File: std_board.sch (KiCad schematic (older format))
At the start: 191 parts, among them IC1 ESP32, IC2 ACS712, IC3 L78L05, IC4 AMS1117-V, J1 Jumper, J10 J_DHT11, J11 Jumper, J12 Jumper, J13 J_PRess, J14 Jumper, J15 Jumper, J16 J_PRess, J17 Jumper, J18 Jumper, J19 Jumper, J2 Jumper, J22 Jumper, J24 Jumper, J25 Jumper, J26 Jumper, J27 Jumper, J29 Jumper, J3 Jumper, J31 Jumper, J32 Jumper, J33 Jumper, J34 Jumper, J35 Jumper, J36 Jumper, J37 Jumper, J38 Jumper, J39 Jumper, J4 Jumper, J40 Jumper, J41 Jumper, J42 Jumper, J43 Jumper, J44 Jumper, J45 Jumper, J5 Jumper, J6 J_PRess, J7 Jumper, J8 Jumper, J9 Jumper, T1 TRIAC_Micro, T2 TRIAC_Micro, T3 TRIAC_Micro, T4 NPN, T5 NPN, T6 NPN, T7 NPN, T8 PNP, T9 NPN, U1 LNK306

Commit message: updates on circuit board and readme file
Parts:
- removed IC1: ESP32, thmalmeida:ESP32_DEVKIT, symbol std_board-rescue:ESP32-thmalmeida
- removed Rectifier1: Bridge_Rectifier, Diode_SMD:Diode_Bridge_Diotec_SO-DIL-Slim, symbol std_board-rescue:Bridge_Rectifier-thmalmeida
- added IC1: ESP32, thmalmeida:ESP32_DEVKIT, symbol thmalmeida:ESP32
- added Rectifier1: DF10S, Package_TO_SOT_SMD:TO-269AA, symbol thmalmeida:Bridge_Rectifier
- C12, C13, C14, C15: value 47 nF -> 10 nF
- C22, C23, C26, C29, C7: footprint thmalmeida:C3_elec_5x4.5_pth -> thmalmeida:C4_elec_7x6.7_pth
- J38: Spice_Model (none) -> Jumper; Spice_Netlist_Enabled (none) -> Y; Spice_Primitive (none) -> X
- R17, R18, R31, R32: value 680 k -> 560 k
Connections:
- net labels added: P10, P11, P12, P13, P15, P33, USB_RX, USB_TX, V_input
- net labels removed: 3V3, L01, L02, L03, L04, L05, L06, L07, L08, L09, L10, L11, L12, L13, L14, L15, R01, R02, R03, R04, R05, R06, R07, R08, R09, R10, R11, R12, R13, R14, R15, R16, R17, Vac_input
- wire segments 562 -> 573
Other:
- note added: "-> V_input = 5 VDC\n-> V_input = [9 - 40] VDC\n-> V_input = [12 - 24] VAC\n-> V_input = [85 -265] VAC"
- note added: "AC load driver"
- note added: "Corner holes for screws"
- note added: "Digital temperature sensor\n (DS18B20)"
- note added: "ESP32, MH-ET live mini board"
- note added: "High-Side, Buck-Direct Feedback"
- note added: "Key features described by manufacturer\n\n1. Output referenced to input;\n2. Positive output (Vo in C point) with respect to -V_input;\n3. Step down -Vo < V_input;\n4. Low cost direct feedback (+-10% typ.);\n5. Requires an output load to maintain regulation."
- note added: "Power circuit protection"
- note added: "RTC DS3231"
- note removed: "Buck"
- note removed: "Circuito de Proteção"
- note removed: "DS3231"
- note removed: "Sensor temperatura (DS18B20)"
- moved on the sheet: +5V_In2, 24Vac_In1, C1, C10, C11, C2, C21, C25, C3, C4, C5, C6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

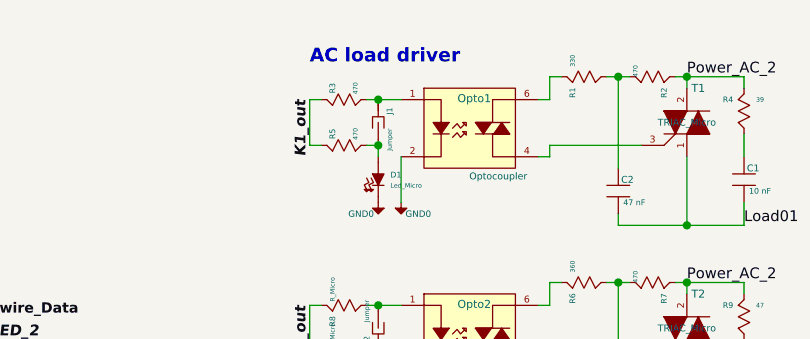
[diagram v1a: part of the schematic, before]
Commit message: AC load explanation
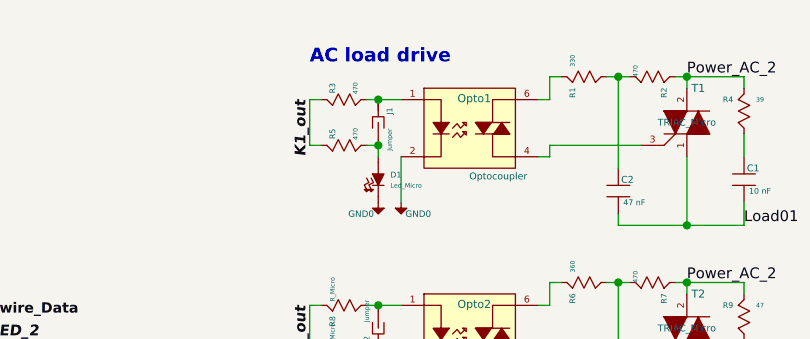
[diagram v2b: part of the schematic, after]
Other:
- note added: "AC load drive"
- note removed: "AC load driver"
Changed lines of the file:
@@
 	800  3550 850  3550
 Text Notes 8950 700  0    60   ~ 12
-AC load driver
+AC load drive
 Wire Wire Line
 	1750 7150 1750 7250

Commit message: TODO list added on REAME.md
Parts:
- AC_Output1, LevelSens_1: symbol thmalmeida:CONN_5X1 -> std_board-rescue:CONN_5X1-thmalmeida
- C10, C11, C8, C9: value 100 nF -> 47 nF
- C22, C23, C24, C26, C27, C29, C7: symbol thmalmeida:CP_Micro -> std_board-rescue:CP_Micro-thmalmeida
- DS3231_1: symbol std_board-rescue:CONN_6X1-thmalmeida -> std_board-rescue:CONN_6X1-thmalmeida-std_board-rescue
- IC1: symbol thmalmeida:ESP32 -> std_board-rescue:ESP32-thmalmeida
- IC3: symbol thmalmeida:L78L05 -> std_board-rescue:L78L05-thmalmeida
- IC4: symbol thmalmeida:AMS1117-V -> std_board-rescue:AMS1117-V-thmalmeida
- Inputs1: symbol thmalmeida:CONN_6X1 -> std_board-rescue:CONN_6X1-thmalmeida
- JTAG1: symbol thmalmeida:JTAG_CONN-06_adapted -> std_board-rescue:JTAG_CONN-06_adapted-thmalmeida
- L1, L2, L4: symbol thmalmeida:L_Micro -> std_board-rescue:L_Micro-thmalmeida
- LS1, LS2: symbol thmalmeida:I_sens -> std_board-rescue:I_sens-thmalmeida
- R20, R21, R22, R23: value 100 k -> 56 k
- R42: value 500 k -> 470 k
- R58: value 3.3 k -> 3.9 k
- Rectifier1: symbol thmalmeida:Bridge_Rectifier -> std_board-rescue:Bridge_Rectifier-thmalmeida
- T8: symbol thmalmeida:PNP -> std_board-rescue:PNP-thmalmeida
- U1: symbol thmalmeida:LNK306 -> std_board-rescue:LNK306-thmalmeida
- Voltimeter_DSO1, currentSource_1: symbol thmalmeida:Connector_2 -> std_board-rescue:Connector_2-thmalmeida
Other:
- note added: "Vrms = 127 V: R42 = 460 k and R58 = 3.9 k"
- note added: "Vrms = 220 V: R42 = 460 k and R58 = 3.9 k"
- moved on the sheet: +5V_In2, D4, J15, J16, J45, R42, R45, R58, R59

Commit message: voltage sensor new structure part 1
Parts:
- removed Voltimeter_DSO1: Voltimeter, TerminalBlock:TerminalBlock_bornier-2_P5.08mm, symbol std_board-rescue:Connector_2-thmalmeida
- added J20, J21, J23: Jumper, thmalmeida:J_0603, symbol std_board-rescue:Jumper-thmalmeida
- added R64: 220 k, Resistor_SMD:R_0805_2012Metric, symbol std_board-rescue:R_Micro-thmalmeida
- AC_Output1: footprint TerminalBlock:TerminalBlock_bornier-5_P5.08mm -> TerminalBlock:TerminalBlock_bornier-6_P5.08mm; symbol std_board-rescue:CONN_5X1-thmalmeida -> std_board-rescue:CONN_6X1-thmalmeida
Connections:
- net Phase_R is gone; now on an unnamed net: J15.2 (B)
- net Common: now also AC_Output1.5, J23.2 (B), R64.1 (A); no longer AC_Output1.1
- net GND: no longer R58.2 (B)
- net Load01: now also AC_Output1.1, J20.1 (A); no longer AC_Output1.5
- net Load02: now also AC_Output1.2; no longer AC_Output1.4
- net Power_AC: now also AC_Output1.4; no longer AC_Output1.2
- net Power_AC_2: now also J15.1 (A)
- net at J45.2 (B), R42.1 (A): now also J20.2 (B), J21.2 (B); no longer J15.1 (A)
- net Neutro: no longer names the net of C24.1, R45.2 (B), R59.1 (A)
- net Neutro: now also R58.2 (B), J23.1 (A), R64.2 (B)
- new net V_external: AC_Output1.6, J21.1 (A)
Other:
- note added: "Common can be\nneutro or one\nreference phase"
- note removed: "Vrms = 220 V: R42 = 460 k and R58 = 3.9 k"
- moved on the sheet: +5V_In2, C24, D4, J15, J16, J45, R42, R45, R58, R59

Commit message: voltage sensor: calculated resistors
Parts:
- removed J27, J29: Jumper, thmalmeida:J_0603, symbol std_board-rescue:Jumper-thmalmeida
- removed T8: PNP, Package_TO_SOT_THT:TO-92, symbol std_board-rescue:PNP-thmalmeida
- added T8: PNP_2N3906, Package_TO_SOT_THT:TO-92, symbol thmalmeida:PNP_TO-92
- Inputs1: value CONN_6X1 -> CONN_5X1; footprint TerminalBlock:TerminalBlock_bornier-6_P5.08mm -> TerminalBlock:TerminalBlock_bornier-5_P5.08mm; symbol std_board-rescue:CONN_6X1-thmalmeida -> std_board-rescue:CONN_5X1-thmalmeida
- R19: value 33 k -> 47 k
- R24: value 1 k -> 2.2 k
- R42: value 470 k -> 680 k
- R58: value 3.9 k -> 3.3 k
- T4, T5, T6, T7, T9: value NPN -> NPN_MMBT222A
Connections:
- net P33 is gone; now on net K3_in: IC1.33 (Wire_SDA/GPIO21_(35))
- net K1_in: now also C8.1 (A), Inputs1.2, R20.2 (B); no longer C9.1 (A), Inputs1.4, R21.2 (B)
- net K2_in: now also C9.1 (A), R21.2 (B); no longer C10.1 (A), R22.2 (B)
- net K3_in: now also C10.1 (A), Inputs1.4, R22.2 (B); no longer C11.1 (A), Inputs1.2, R23.2 (B)
- net L1_in: now also J4.1 (A), J7.2 (B), R17.2 (B), T4.3 (C); no longer J12.1 (A), J22.2 (B), R32.1 (A), T7.3 (C)
- net L1_probe: now also C12.1 (A), J4.2 (B), LevelSens_1.2, R25.1 (A), R27.1 (A); no longer C15.1 (A), J12.2 (B), LevelSens_1.1, R35.1 (A), R37.1 (A)
- net L2_in: now also J26.2 (B), J5.1 (A), R18.2 (B), T5.3 (C); no longer J11.1 (A), J25.2 (B), R31.1 (A), T6.3 (C)
- net L2_probe: now also C13.1 (A), J5.2 (B), LevelSens_1.3, R26.1 (A), R28.1 (A); no longer C14.1 (A), J11.2 (B), LevelSens_1.2, R34.1 (A), R36.1 (A)
- net L3_in: now also J11.1 (A), J25.2 (B), R31.1 (A), T6.3 (C); no longer J26.2 (B), J5.1 (A), R18.2 (B), T5.3 (C)
- net L3_probe: now also C14.1 (A), J11.2 (B), LevelSens_1.4, R34.1 (A), R36.1 (A); no longer C13.1 (A), J5.2 (B), LevelSens_1.3, R26.1 (A), R28.1 (A)
- net L4_in: now also J12.1 (A), J22.2 (B), R32.1 (A), T7.3 (C); no longer J4.1 (A), J7.2 (B), R17.2 (B), T4.3 (C)
- net L4_probe: now also C15.1 (A), J12.2 (B), LevelSens_1.5, R35.1 (A), R37.1 (A); no longer C12.1 (A), J4.2 (B), LevelSens_1.4, R25.1 (A), R27.1 (A)
- net T1_in: now also C11.1 (A), R23.2 (B); no longer C8.1 (A), R20.2 (B)
- net at D7.2 (-Cathode), J9.1 (A): now also LevelSens_1.1; no longer LevelSens_1.5
- net at R24.1 (A): now also T8.2 (B)
- net at J34.2 (B), J37.2 (B), R19.2 (B): now also T8.1 (E)
- net at currentSource_1.1 (S1): now also T8.3 (C)
- removed net T2_in: Inputs1.6
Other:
- note added: "Fórmula: R1/(R2+R1)*Vrms*sqrt(2)+3.3/2"
- note added: "Vmax read = 138 Vrms"
- note added: "Vmax read = 241 Vrms"
- note added: "Vrms = 220 V: R42 = 680 k and R58 = 3.3 k"
- moved on the sheet: C10, C11, C8, C9, R20, R21, R22, R23

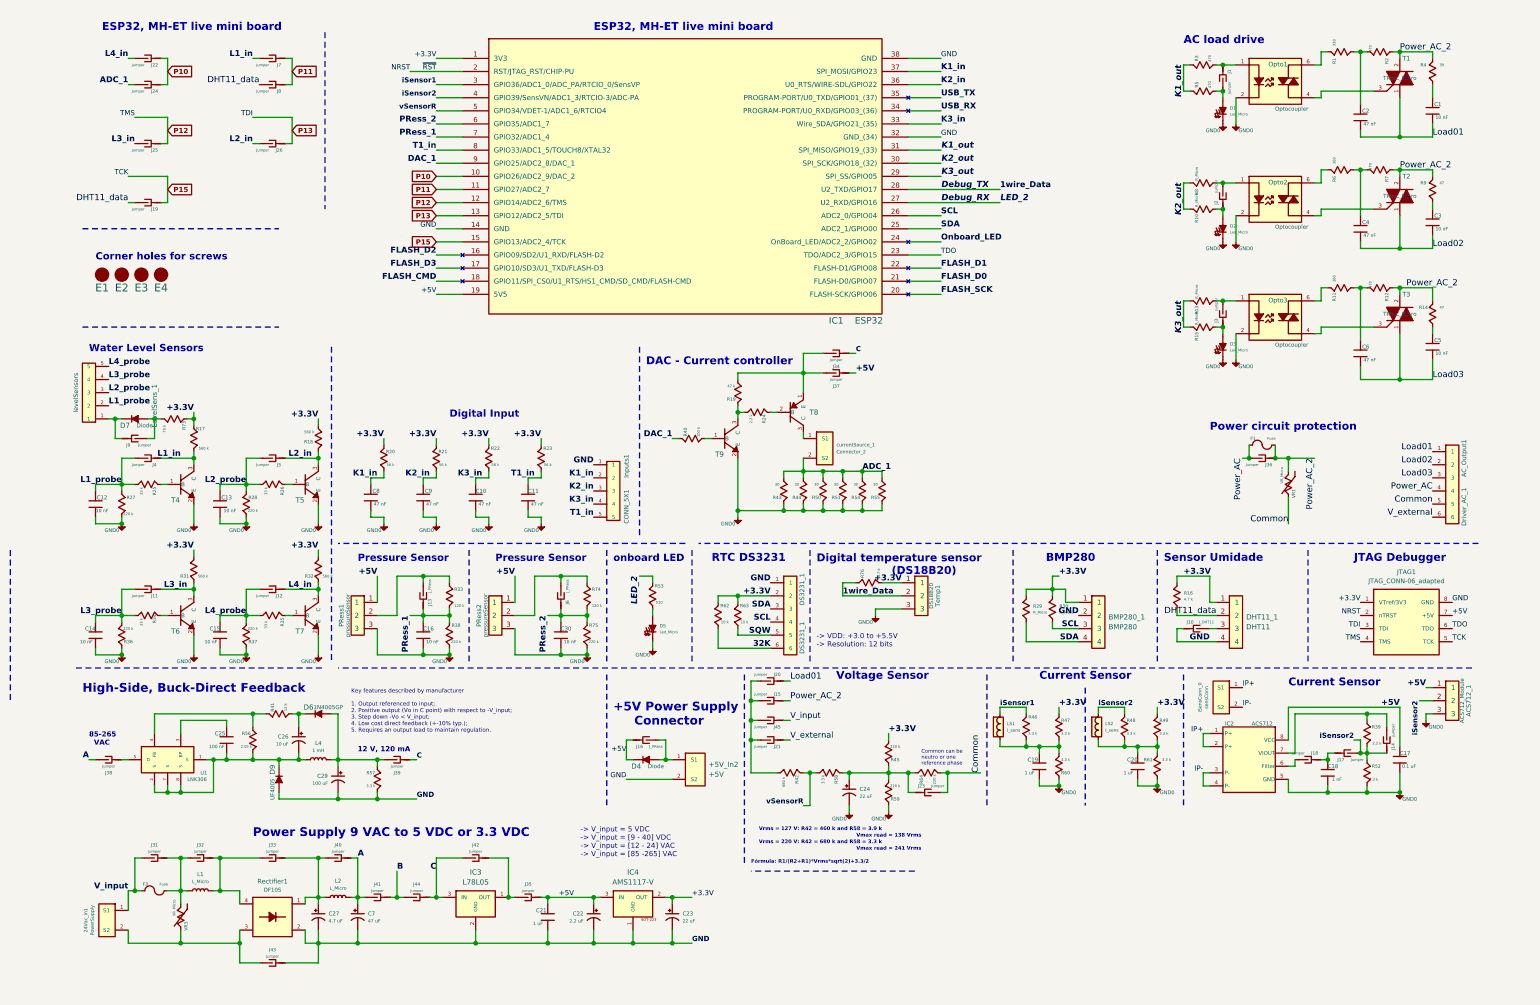
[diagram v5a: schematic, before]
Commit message: fixed voltage divider of pressure circuit design
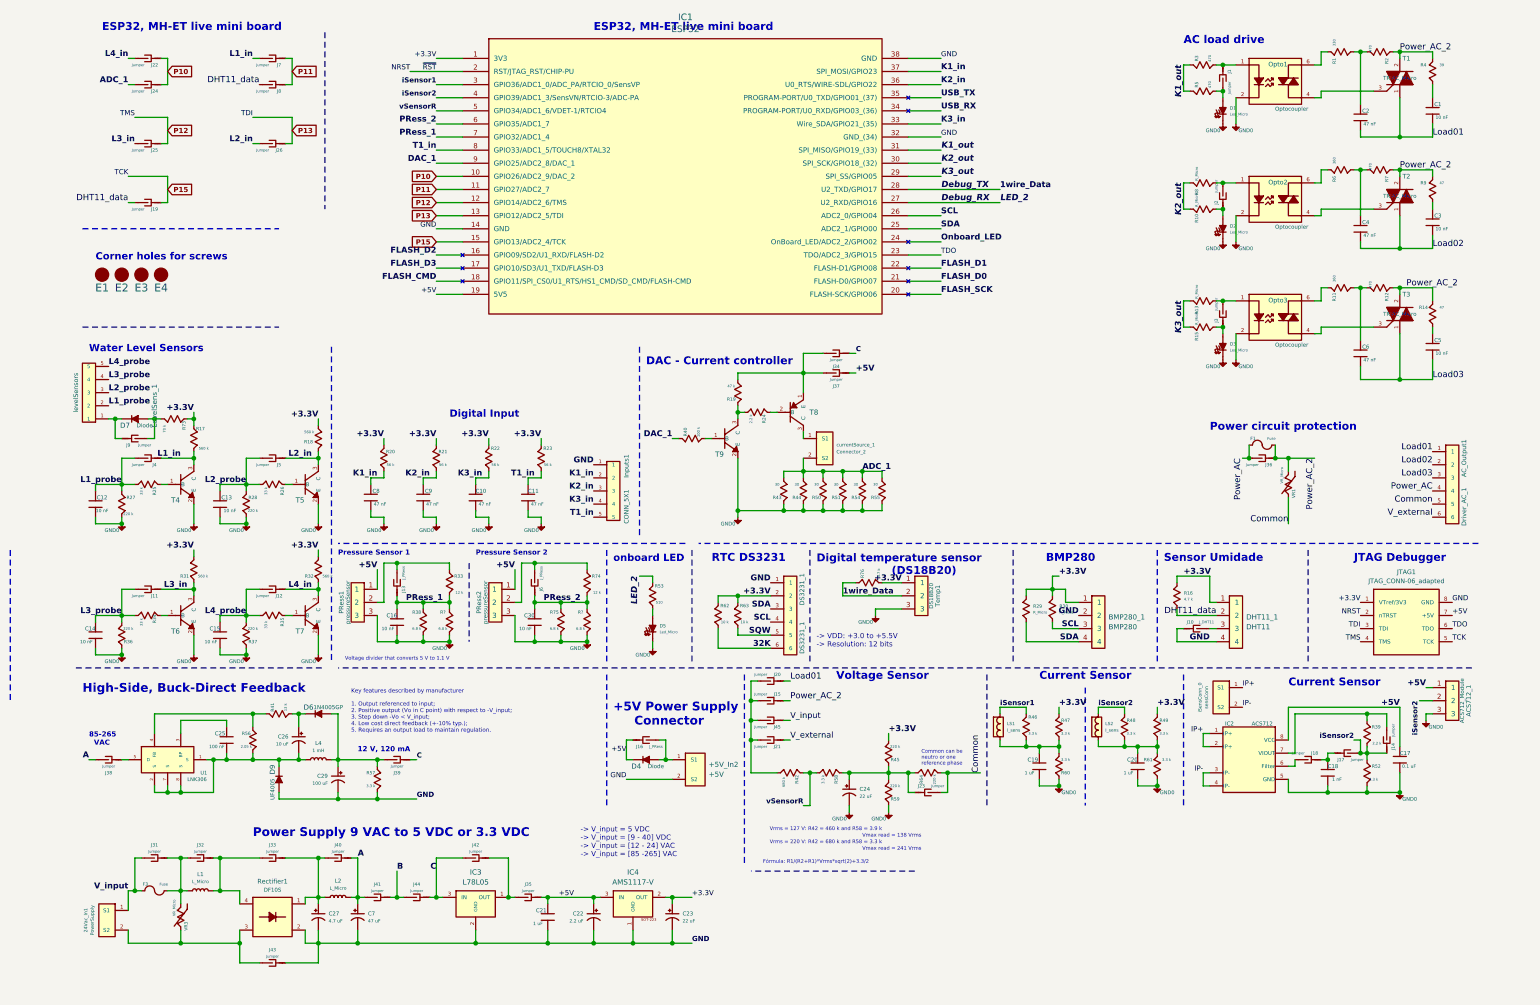
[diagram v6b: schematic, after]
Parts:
- removed IC1: ESP32, thmalmeida:ESP32_DEVKIT, symbol std_board-rescue:ESP32-thmalmeida
- added IC1: ESP32, thmalmeida:ESP32_DEVKIT, symbol thmalmeida:ESP32
- added R? (x2): 6.8 k, Resistor_SMD:R_0805_2012Metric, symbol std_board-rescue:R_Micro-thmalmeida
- R33, R74: value 120 k -> 12 k
- R38, R75: value 220 k -> 6.8 k
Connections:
- net +3.3V: now also IC1.1 (3V3)
- net +5V: now also IC1.19 (5V5)
- net 1wire_Data: now also IC1.28 (U2_TXD/GPIO17)
- net DAC_1: now also IC1.9 (GPIO25/ADC2_8/DAC_1)
- net Debug_RX: now also IC1.27 (U2_RXD/GPIO16)
- net FLASH_CMD: now also IC1.18 (GPIO11/SPI_CS0/U1_RTS/HS1_CMD/SD_CMD/FLASH-CMD)
- net FLASH_D0: now also IC1.21 (FLASH-D0/GPIO07)
- net FLASH_D1: now also IC1.22 (FLASH-D1/GPIO08)
- net FLASH_D2: now also IC1.16 (GPIO09/SD2/U1_RXD/FLASH-D2)
- net FLASH_D3: now also IC1.17 (GPIO10/SD3/U1_TXD/FLASH-D3)
- net FLASH_SCK: now also IC1.20 (FLASH-SCK/GPIO06)
- net GND: now also IC1.14 (GND), IC1.32 (GND_(34)), IC1.38 (GND), R?.2 (B), R?.2 (B)
- net K1_in: now also IC1.37 (SPI_MOSI/GPIO23)
- net K1_out: now also IC1.31 (SPI_MISO/GPIO19_(33))
- net K2_in: now also IC1.36 (U0_RTS/WIRE-SDL/GPIO22)
- net K2_out: now also IC1.30 (SPI_SCK/GPIO18_(32))
- net K3_in: now also IC1.33 (Wire_SDA/GPIO21_(35))
- net K3_out: now also IC1.29 (SPI_SS/GPIO05)
- net NRST: now also IC1.2 (RST/JTAG_RST/CHIP-PU)
- net Onboard_LED: now also IC1.24 (OnBoard_LED/ADC2_2/GPIO02)
- net P10: now also IC1.10 (GPIO26/ADC2_9/DAC_2)
- net P11: now also IC1.11 (GPIO27/ADC2_7)
- net P12: now also IC1.12 (GPIO14/ADC2_6/TMS)
- net P13: now also IC1.13 (GPIO12/ADC2_5/TDI)
- net P15: now also IC1.15 (GPIO13/ADC2_4/TCK)
- net PRess_1: now also IC1.7 (GPIO32/ADC1_4), R?.1 (A)
- net PRess_2: now also IC1.6 (GPIO35/ADC1_7), R?.1 (A)
- net SCL: now also IC1.26 (ADC2_0/GPIO04)
- net SDA: now also IC1.25 (ADC2_1/GPIO00)
- net T1_in: now also IC1.8 (GPIO33/ADC1_5/TOUCH8/XTAL32)
- net TDO: now also IC1.23 (TDO/ADC2_3/GPIO15)
- net USB_RX: now also IC1.34 (PROGRAM-PORT/U0_RXD/GPIO03_(36))
- net USB_TX: now also IC1.35 (PROGRAM-PORT/U0_TXD/GPIO01_(37))
- net iSensor1: now also IC1.3 (GPIO36/ADC1_0/ADC_PA/RTCIO_0/SensVP)
- net iSensor2: now also IC1.4 (GPIO39/ADC1_3/SensVN/RTCIO-3/ADC-PA)
- net vSensorR: now also IC1.5 (GPIO34/ADC1_6/VDET-1/RTCIO4)
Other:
- note added: "Pressure Sensor 1"
- note added: "Pressure Sensor 2"
- note added: "Voltage divider that converts 5 V to 1.1 V"
- note removed: "Pressure Sensor"
- moved on the sheet: C16, C30, J13, J6, PRess1, PRess2, R33, R38, R74, R75

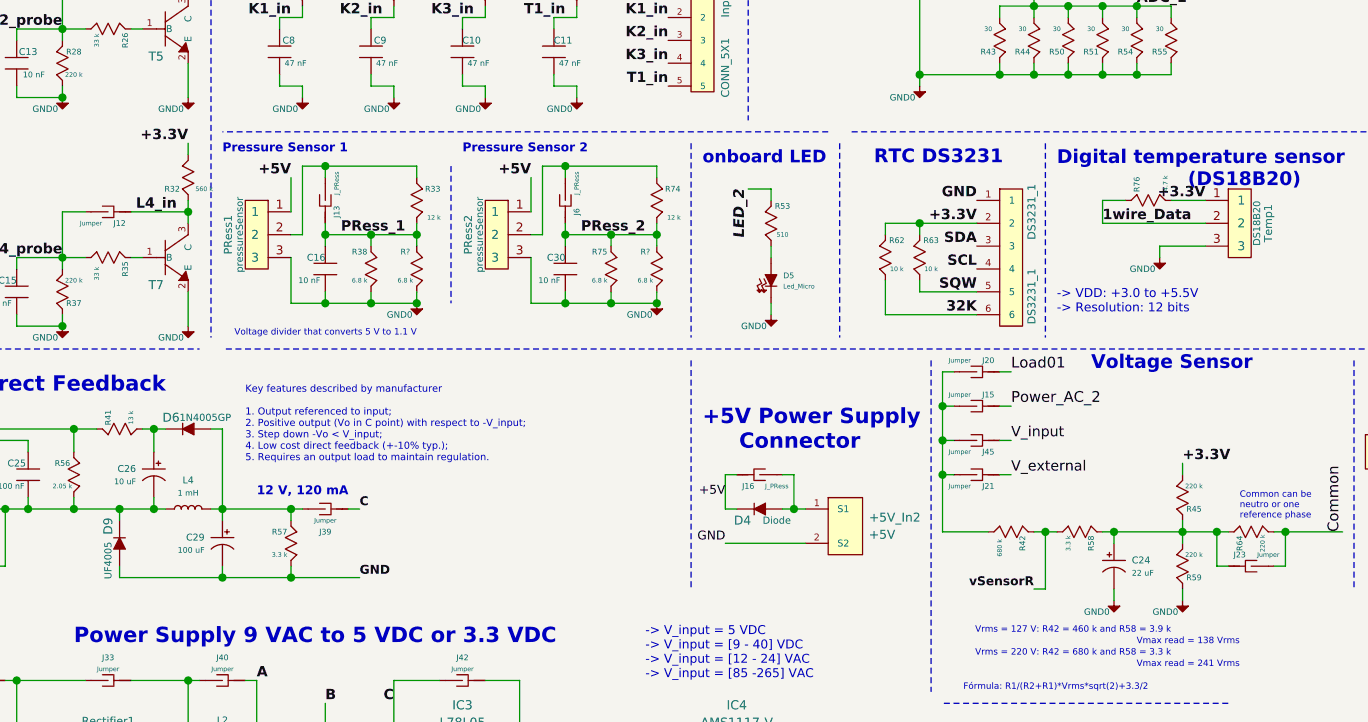
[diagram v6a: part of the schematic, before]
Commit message: recalculated ADC voltage divider measurement
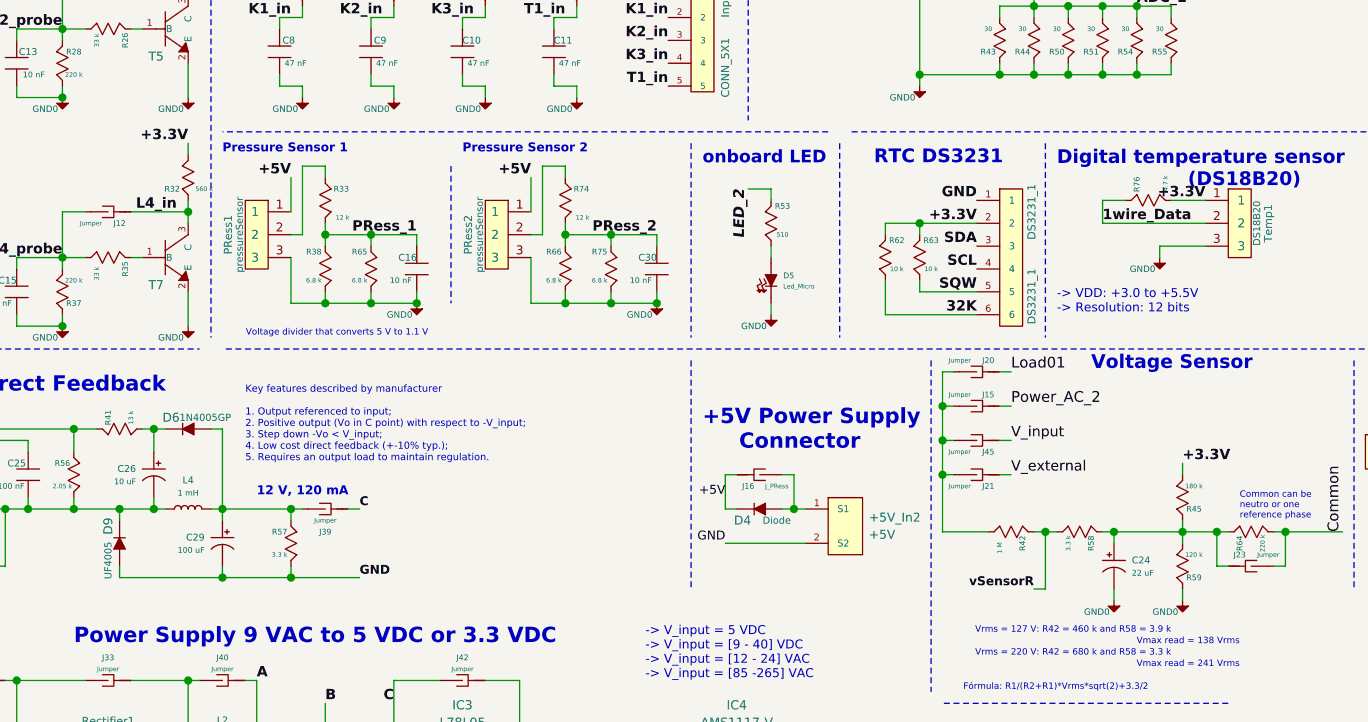
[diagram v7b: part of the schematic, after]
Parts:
- removed J13, J6: J_PRess, thmalmeida:J_0603, symbol std_board-rescue:Jumper-thmalmeida
- R42: value 680 k -> 1 M
- R45: value 220 k -> 180 k
- R59: value 220 k -> 120 k
- gave numbers to parts that had none: 2
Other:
- moved on the sheet: C16, C30, R33, R38, R65, R66, R74
